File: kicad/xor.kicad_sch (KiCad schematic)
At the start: 1 part, among them U2 4070

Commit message: update part numbers
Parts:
- U2: manf# (none) -> CD4070BE
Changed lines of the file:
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@@
 		(shape input)
 		(at 106.68 90.17 180)
+		(fields_autoplaced yes)
 		(effects
 			(font
@@
 		(shape output)
 		(at 137.16 92.71 0)
+		(fields_autoplaced yes)
 		(effects
 			(font
@@
 		(shape input)
 		(at 106.68 95.25 180)
+		(fields_autoplaced yes)
 		(effects
 			(font
@@
 		(shape input)
 		(at 106.68 71.12 180)
+		(fields_autoplaced yes)
 		(effects
 			(font
@@
 		(shape input)
 		(at 106.68 53.34 180)
+		(fields_autoplaced yes)
 		(effects
 			(font
@@
 		(shape output)
 		(at 137.16 68.58 0)
+		(fields_autoplaced yes)
 		(effects
 			(font
@@
 		(shape input)
 		(at 106.68 82.55 180)
+		(fields_autoplaced yes)
 		(effects
 			(font
@@
 		(shape output)
 		(at 137.16 80.01 0)
+		(fields_autoplaced yes)
 		(effects
 			(font
@@
 		(shape input)
 		(at 106.68 66.04 180)
+		(fields_autoplaced yes)
 		(effects
 			(font
@@
 		(shape input)
 		(at 106.68 77.47 180)
+		(fields_autoplaced yes)
 		(effects
 			(font
@@
 		(shape input)
 		(at 106.68 58.42 180)
+		(fields_autoplaced yes)
 		(effects
 			(font
@@
 		(shape output)
 		(at 137.16 55.88 0)
+		(fields_autoplaced yes)
 		(effects
 			(font
@@
 			)
 		)
+		(property "manf#" "CD4070BE"
+			(at 121.92 55.88 0)
+			(effects
+				(font
+					(size 1.27 1.27)
+				)
+				(hide yes)
+			)
+		)
 		(pin "14"
 		)
@@
 			)
 		)
+		(property "manf#" "CD4070BE"
+			(at 121.92 68.58 0)
+			(effects
+				(font
+					(size 1.27 1.27)
+				)
+				(hide yes)
+			)
+		)
 		(pin "14"
 		)
@@
 			)
 		)
+		(property "manf#" "CD4070BE"
+			(at 121.92 80.01 0)
+			(effects
+				(font
+					(size 1.27 1.27)
+				)
+				(hide yes)
+			)
+		)
 		(pin "14"
 		)
@@
 			(at 121.92 92.71 0)
 			(effects
+				(font
+					(size 1.27 1.27)
+				)
+				(hide yes)
+			)
+		)
+		(property "manf#" "CD4070BE"
+			(at 121.92 92.71 0)
+			(effects

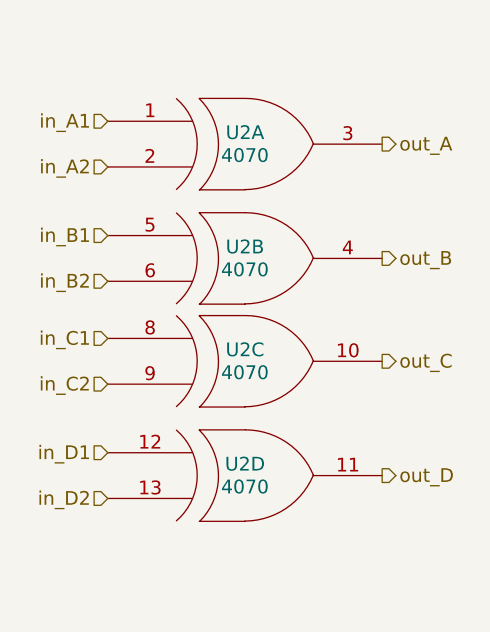
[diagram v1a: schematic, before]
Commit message: change pots
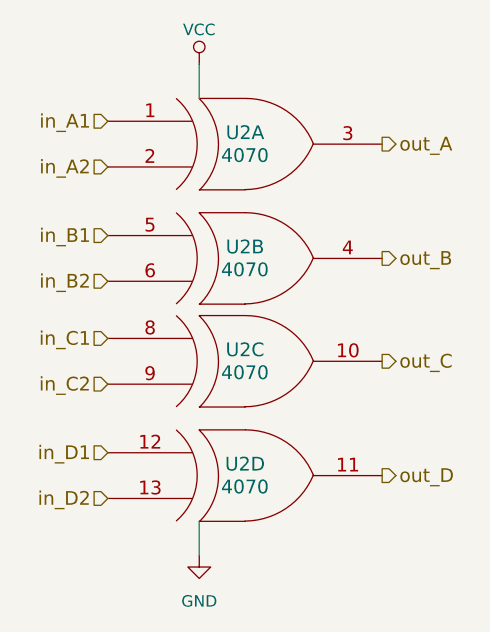
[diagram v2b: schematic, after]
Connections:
- net VDD renamed VCC
- net VSS renamed GND
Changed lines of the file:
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@@
 	(generator_version "8.0")
 	(paper "A4")
+	(wire
+		(pts
+			(xy 116.84 46.99) (xy 116.84 50.8)
+		)
+		(stroke
+			(width 0)
+			(type default)
+		)
+	)
+	(wire
+		(pts
+			(xy 116.84 101.6) (xy 116.84 97.79)
+		)
+		(stroke
+			(width 0)
+			(type default)
+		)
+	)
 	(hierarchical_label "in_D1"
 		(shape input)
@@
 				)
 			)
+		)
+	)
+	(symbol
+		(lib_id "power:GND")
+		(at 116.84 101.6 0)
+		(unit 1)
+		(exclude_from_sim no)
+		(in_bom yes)
+		(on_board yes)
+		(dnp no)
+		(fields_autoplaced yes)
+		(property "Reference" "#PWR049"
+			(at 116.84 107.95 0)
+			(effects
+				(font
+					(size 1.27 1.27)
+				)
+				(hide yes)
+			)
+		)
+		(property "Value" "GND"
+			(at 116.84 106.68 0)
+			(effects
+				(font
+					(size 1.27 1.27)
+				)
+			)
+		)
+		(property "Footprint" ""
+			(at 116.84 101.6 0)
+			(effects
+				(font
+					(size 1.27 1.27)
+				)
+				(hide yes)
+			)
+		)
+		(property "Datasheet" ""
+			(at 116.84 101.6 0)
+			(effects
+				(font
+					(size 1.27 1.27)
+				)
+				(hide yes)
+			)
+		)
+		(property "Description" "Power symbol creates a global label with name \"GND\" , ground"
+			(at 116.84 101.6 0)
+			(effects
+				(font
+					(size 1.27 1.27)
+				)
+				(hide yes)
+			)
+		)
+		(pin "1"
+		)
+		(instances
+			(project "logic_noise_playground"
+				(path "/b9341db6-1cc2-4b11-8dd1-ce51623beade/00000000-0000-0000-0000-0000554d4d64"
+					(reference "#PWR049")
+					(unit 1)
+				)
+			)
+		)
+	)
+	(symbol
+		(lib_id "logic_noise_playground-rescue:VCC")
+		(at 116.84 46.99 0)
+		(unit 1)
+		(exclude_from_sim no)
+		(in_bom yes)
+		(on_board yes)
+		(dnp no)
+		(property "Reference" "#PWR048"
+			(at 116.84 50.8 0)
+			(effects
+				(font
+					(size 1.27 1.27)
+				)
+				(hide yes)
+			)
+		)
+		(property "Value" "VCC"
+			(at 116.84 43.18 0)
+			(effects
+				(font
+					(size 1.27 1.27)
+				)
+			)
+		)
+		(property "Footprint" ""
+			(at 116.84 46.99 0)
+			(effects
+				(font
+					(size 1.524 1.524)
+				)
+			)
+		)
+		(property "Datasheet" ""
+			(at 116.84 46.99 0)
+			(effects
+				(font
+					(size 1.524 1.524)
+				)
+			)
+		)
+		(property "Description" ""
+			(at 116.84 46.99 0)
+			(effects
+				(font
+					(size 1.27 1.27)
+				)
+				(hide yes)
+			)
+		)
+		(pin "1"
+		)
+		(instances
+			(project "logic_noise_playground"
+				(path "/b9341db6-1cc2-4b11-8dd1-ce51623beade/00000000-0000-0000-0000-0000554d4d64"
+					(reference "#PWR048")
+					(unit 1)
+				)
+			)

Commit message: update to kicad 9, add some comments and circuit changes
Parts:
- U2: Orden (none) -> 99
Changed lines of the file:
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@@
 		(shape input)
 		(at 106.68 90.17 180)
-		(fields_autoplaced yes)
 		(effects
 			(font
@@
 		(shape output)
 		(at 137.16 92.71 0)
-		(fields_autoplaced yes)
 		(effects
 			(font
@@
 		(shape input)
 		(at 106.68 95.25 180)
-		(fields_autoplaced yes)
 		(effects
 			(font
@@
 		(shape input)
 		(at 106.68 71.12 180)
-		(fields_autoplaced yes)
 		(effects
 			(font
@@
 		(shape input)
 		(at 106.68 53.34 180)
-		(fields_autoplaced yes)
 		(effects
 			(font
@@
 		(shape output)
 		(at 137.16 68.58 0)
-		(fields_autoplaced yes)
 		(effects
 			(font
@@
 		(shape input)
 		(at 106.68 82.55 180)
-		(fields_autoplaced yes)
 		(effects
 			(font
@@
 		(shape output)
 		(at 137.16 80.01 0)
-		(fields_autoplaced yes)
 		(effects
 			(font
@@
 		(shape input)
 		(at 106.68 66.04 180)
-		(fields_autoplaced yes)
 		(effects
 			(font
@@
 		(shape input)
 		(at 106.68 77.47 180)
-		(fields_autoplaced yes)
 		(effects
 			(font
@@
 		(shape input)
 		(at 106.68 58.42 180)
-		(fields_autoplaced yes)
 		(effects
 			(font
@@
 		(shape output)
 		(at 137.16 55.88 0)
-		(fields_autoplaced yes)
 		(effects
 			(font
@@
 			)
 		)
+		(property "Orden" "99"
+			(at 121.92 55.88 0)
+			(effects
+				(font
+					(size 1.27 1.27)
+				)
+				(hide yes)
+			)
+		)
+		(property "Comentarios" ""
+			(at 121.92 55.88 0)
+			(effects
+				(font
+					(size 1.27 1.27)
+				)
+				(hide yes)
+			)
+		)
 		(pin "14"
 		)
@@
 			)
 		)
+		(property "Orden" "99"
+			(at 121.92 68.58 0)
+			(effects
+				(font
+					(size 1.27 1.27)
+				)
+				(hide yes)
+			)
+		)
+		(property "Comentarios" ""
+			(at 121.92 68.58 0)
+			(effects
+				(font
+					(size 1.27 1.27)
+				)
+				(hide yes)
+			)
+		)
 		(pin "14"
 		)
@@
 			)
 		)
+		(property "Orden" "99"
+			(at 121.92 80.01 0)
+			(effects
+				(font
+					(size 1.27 1.27)
+				)
+				(hide yes)
+			)
+		)
+		(property "Comentarios" ""
+			(at 121.92 80.01 0)
+			(effects
+				(font
+					(size 1.27 1.27)
+				)
+				(hide yes)
+			)
+		)
 		(pin "14"
 		)
@@
 			(at 121.92 92.71 0)
 			(effects
+				(font
+					(size 1.27 1.27)
+				)
+				(hide yes)
+			)
+		)
+		(property "Orden" "99"
+			(at 121.92 92.71 0)
+			(effects
+				(font
+					(size 1.27 1.27)
+				)
+				(hide yes)
+			)
+		)
+		(property "Comentarios" ""
+			(at 121.92 92.71 0)
+			(effects
